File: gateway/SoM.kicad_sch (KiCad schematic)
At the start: 20 parts, among them SW901 Reset, SW902 On / Off, X901 SoM, X902 UART

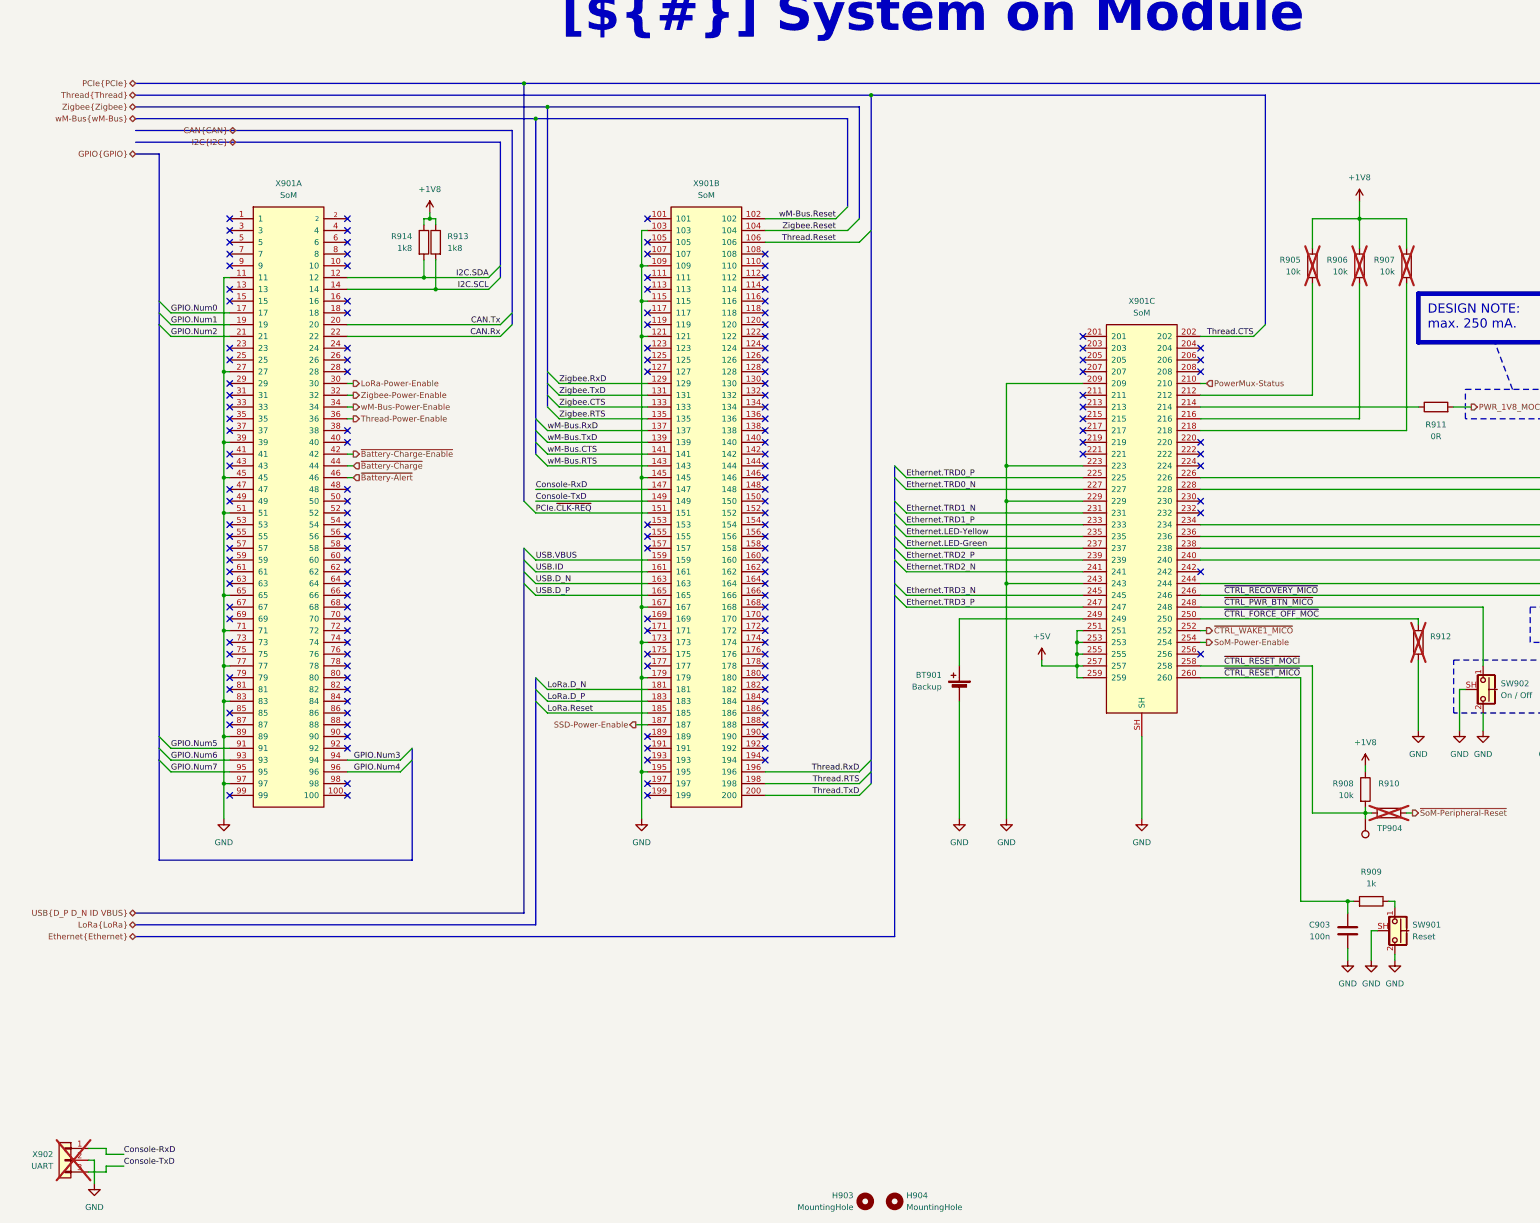
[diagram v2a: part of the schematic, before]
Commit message: Replace level shifter, replace CC2530 with CC2652, fix wrong part numbers
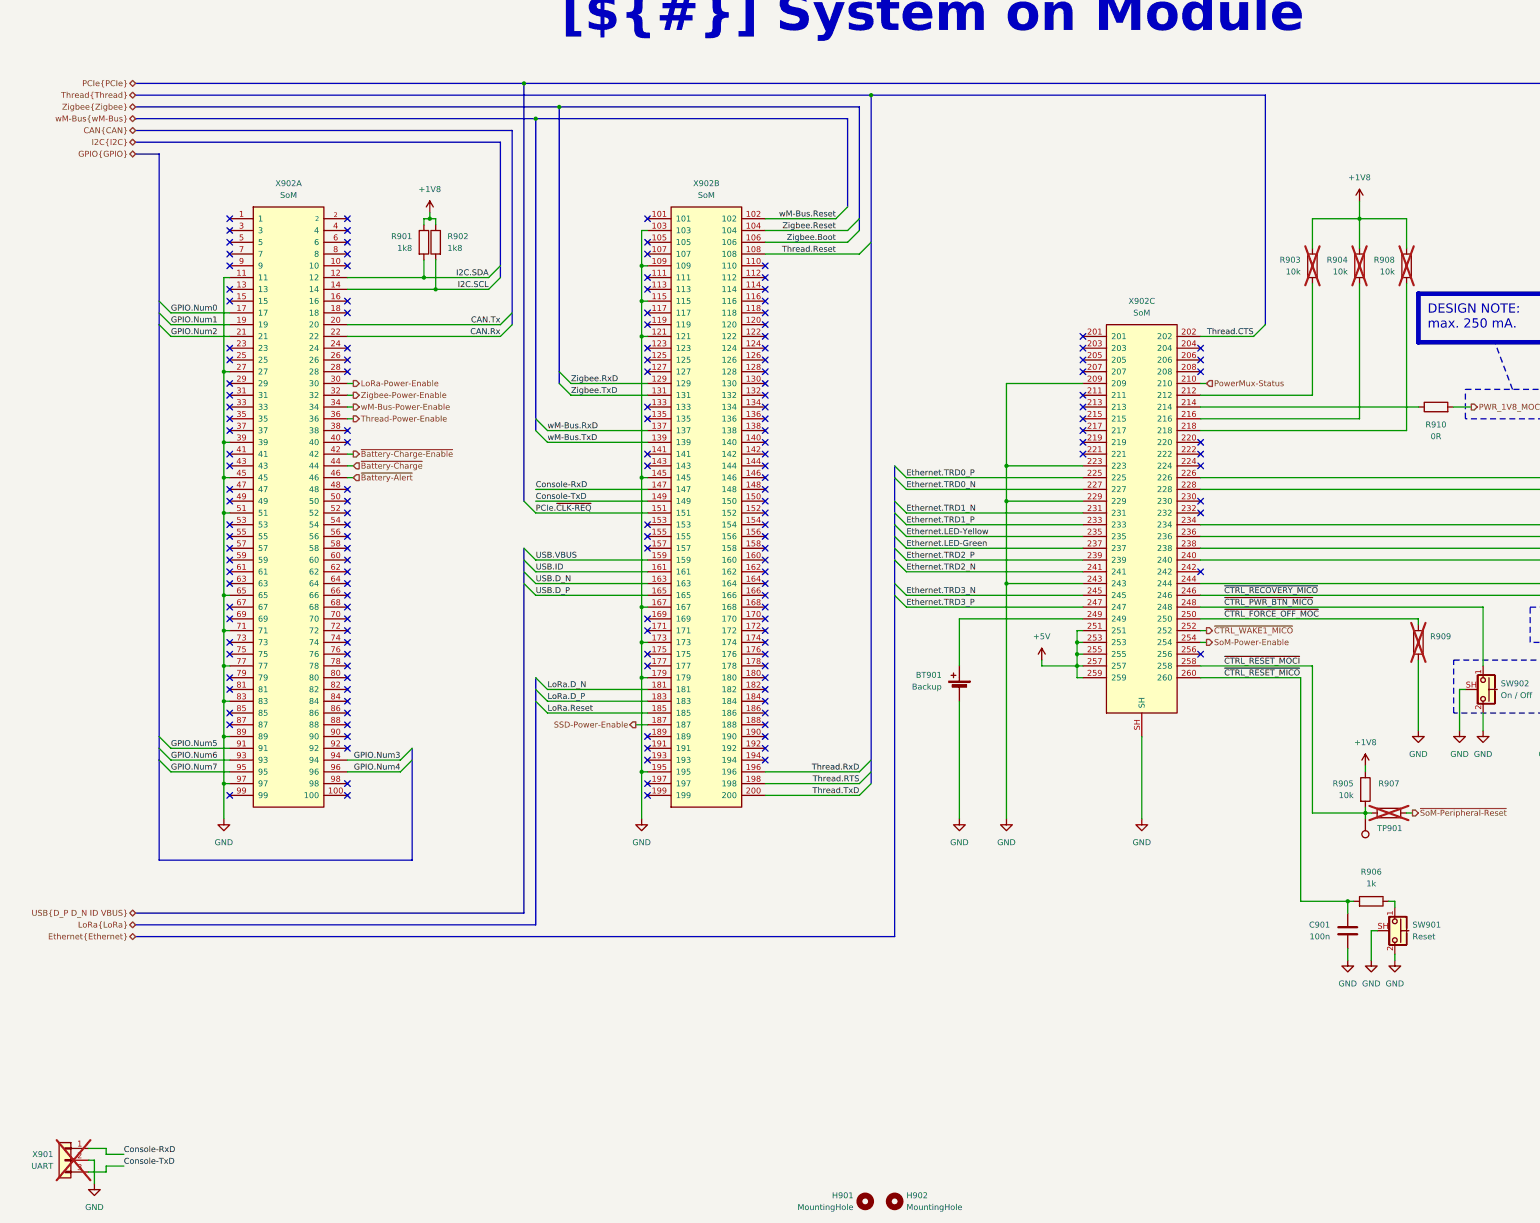
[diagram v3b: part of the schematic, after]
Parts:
- renumbered C903 to C901, H903 to H901, H904 to H902, R914 to R901, R913 to R902, R905 to R903, R906 to R904, R908 to R905, R909 to R906, R910 to R907, R907 to R908, R912 to R909, R911 to R910, TP904 to TP901, X902 to X901, X901 to X902
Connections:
- net Thread.Reset: now also X902.108; no longer X902.106
- net Zigbee.CTS: no longer names the net of X902.133
- net Zigbee.RTS: no longer names the net of X902.135
- net wM-Bus.CTS: no longer names the net of X902.141
- net wM-Bus.RTS: no longer names the net of X902.143
- new net Zigbee.Boot: X902.106
- no-connect marks 156 -> 159
